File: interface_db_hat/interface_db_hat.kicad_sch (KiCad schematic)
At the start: 37 parts, among them J10 Conn_02x06_Counter_Clockwise, J2 DF19G-20P-1H52, J3 Conn_02x06_Counter_Clockwise, J6 Conn_01x04_Pin, J9 Conn_02x06_Counter_Clockwise, Q1 BC817

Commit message: ordered
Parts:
- C31, C34, C46: footprint Capacitor_SMD:C_0603_1608Metric_Pad1.08x0.95mm_HandSolder -> Capacitor_SMD:C_0805_2012Metric
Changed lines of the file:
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@@
 			)
 		)
-		(property "Footprint" "Capacitor_SMD:C_0603_1608Metric_Pad1.08x0.95mm_HandSolder"
+		(property "Footprint" "Capacitor_SMD:C_0805_2012Metric"
 			(at 147.0152 157.48 0)
 			(hide yes)
@@
 			)
 		)
-		(property "Footprint" "Capacitor_SMD:C_0603_1608Metric_Pad1.08x0.95mm_HandSolder"
+		(property "Footprint" "Capacitor_SMD:C_0805_2012Metric"
 			(at 84.7852 180.34 0)
 			(hide yes)
@@
 			)
 		)
-		(property "Footprint" "Capacitor_SMD:C_0603_1608Metric_Pad1.08x0.95mm_HandSolder"
+		(property "Footprint" "Capacitor_SMD:C_0805_2012Metric"
 			(at 84.7852 133.35 0)
 			(hide yes)

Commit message: update
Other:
- added sheet photodiode (photodiode.kicad_sch)
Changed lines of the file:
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@@
+	)
+	(sheet
+		(at 110.49 170.815)
+		(size 46.99 21.59)
+		(exclude_from_sim no)
+		(in_bom yes)
+		(on_board yes)
+		(dnp no)
+		(fields_autoplaced yes)
+		(stroke
+			(width 0.1524)
+			(type solid)
+		)
+		(fill
+			(color 0 0 0 0)
+		)
+		(property "Sheetname" "photodiode"
+			(at 110.49 170.1034 0)
+			(show_name no)
+			(do_not_autoplace no)
+			(effects
+				(font
+					(size 1.27 1.27)
+				)
+				(justify left bottom)
+			)
+		)
+		(property "Sheetfile" "photodiode.kicad_sch"
+			(at 110.49 192.9896 0)
+			(show_name no)
+			(do_not_autoplace no)
+			(effects
+				(font
+					(size 1.27 1.27)
+				)
+				(justify left top)
+			)
+		)
+		(instances
+			(project "interface_db_hat"
+				(path "/e63e39d7-6ac0-4ffd-8aa3-1841a4541b55"
+					(page "5")
+				)
+			)
+		)
 	)
 	(sheet

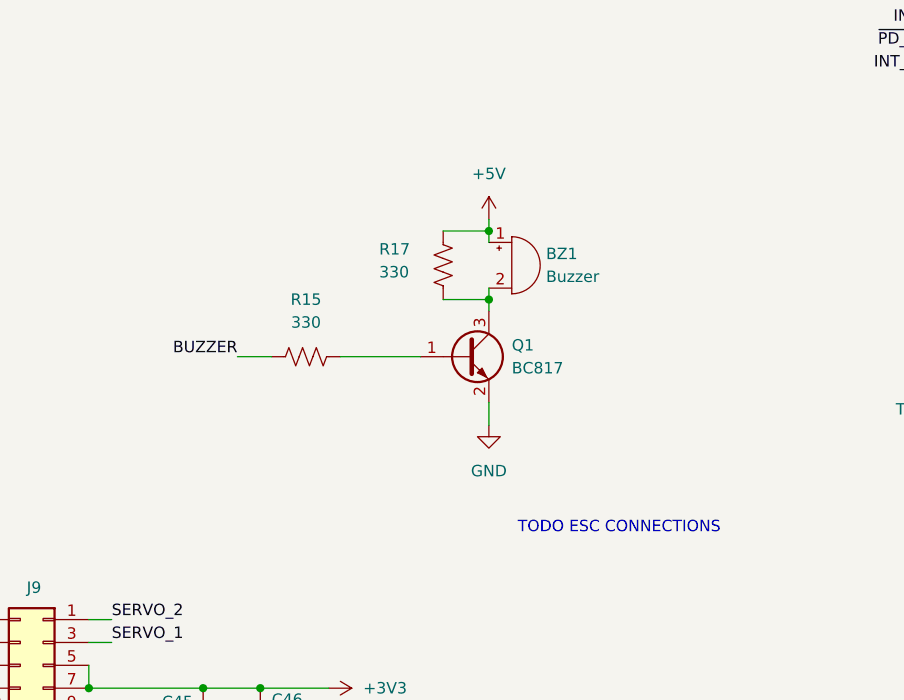
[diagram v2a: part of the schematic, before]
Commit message: starting interface layout
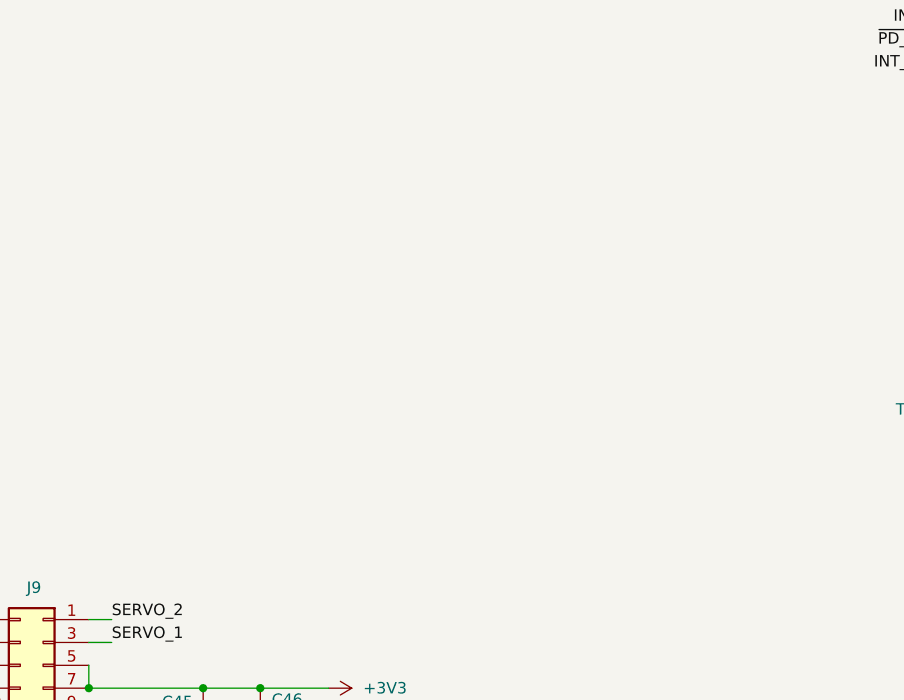
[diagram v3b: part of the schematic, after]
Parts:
- removed BZ1: Buzzer, Buzzer_Beeper:Buzzer_CUI_CPT-9019S-SMT, symbol Device:Buzzer
- removed Q1: BC817, Package_TO_SOT_SMD:SOT-23_Handsoldering, symbol Transistor_BJT:BC817
- removed R15, R17: 330, Resistor_SMD:R_0603_1608Metric_Pad0.98x0.95mm_HandSolder, symbol Device:R_US
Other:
- note removed: "TODO ESC CONNECTIONS"

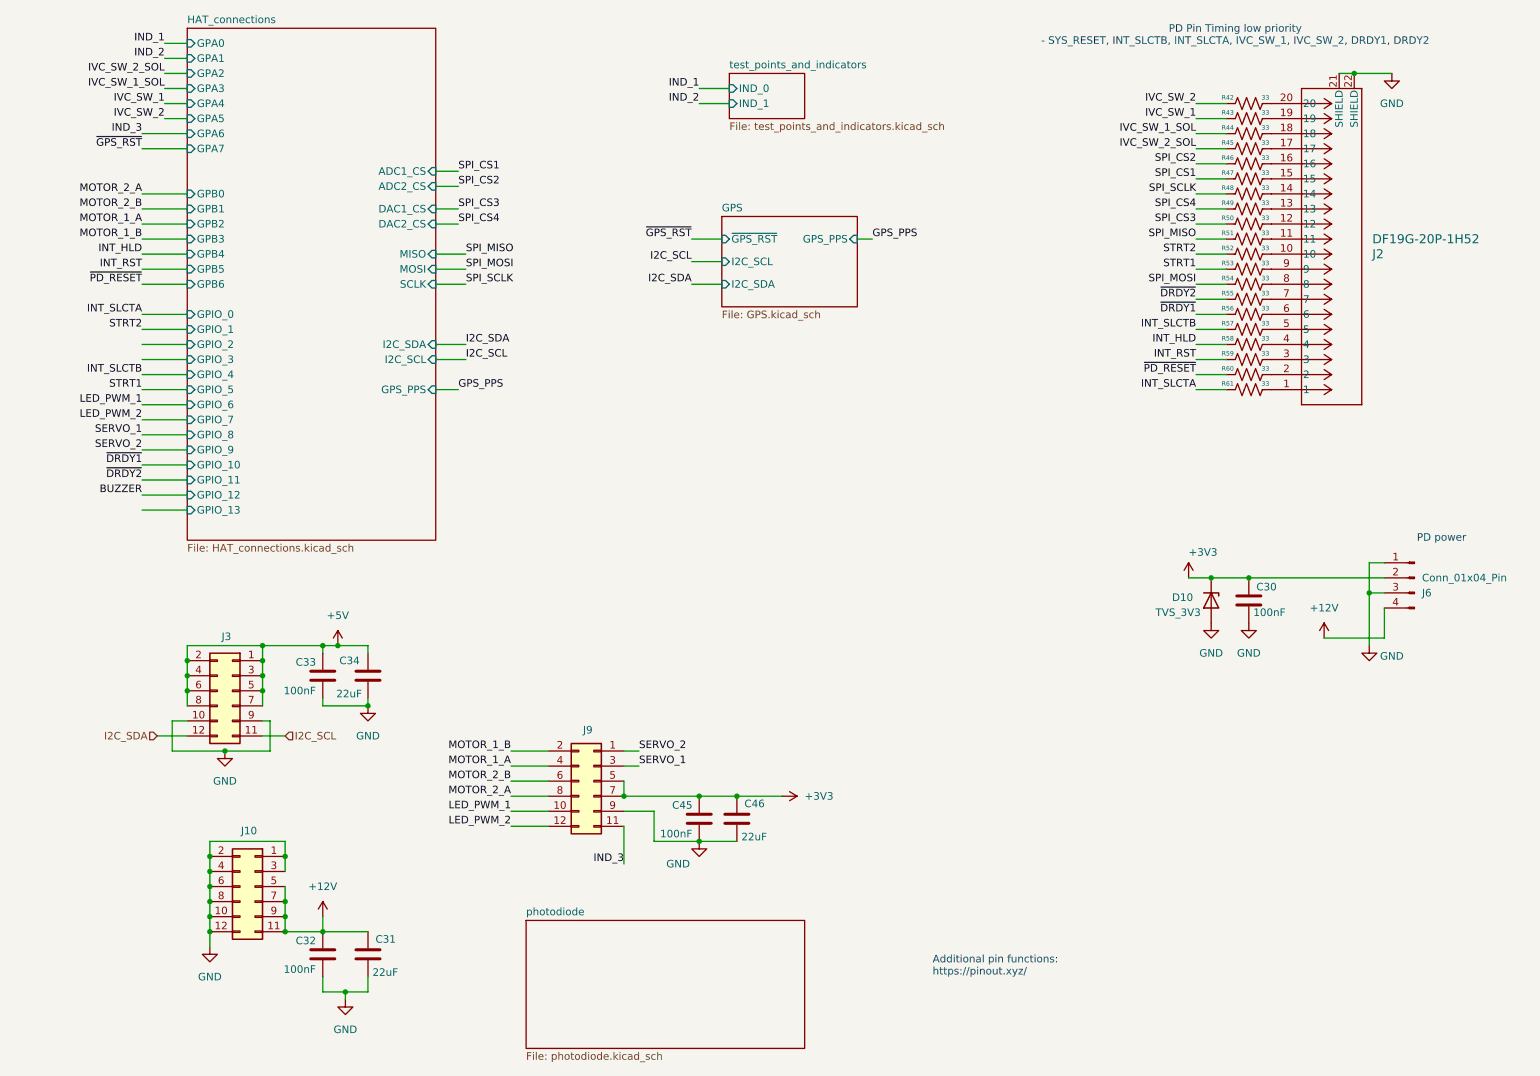
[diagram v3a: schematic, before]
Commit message: interface layout done
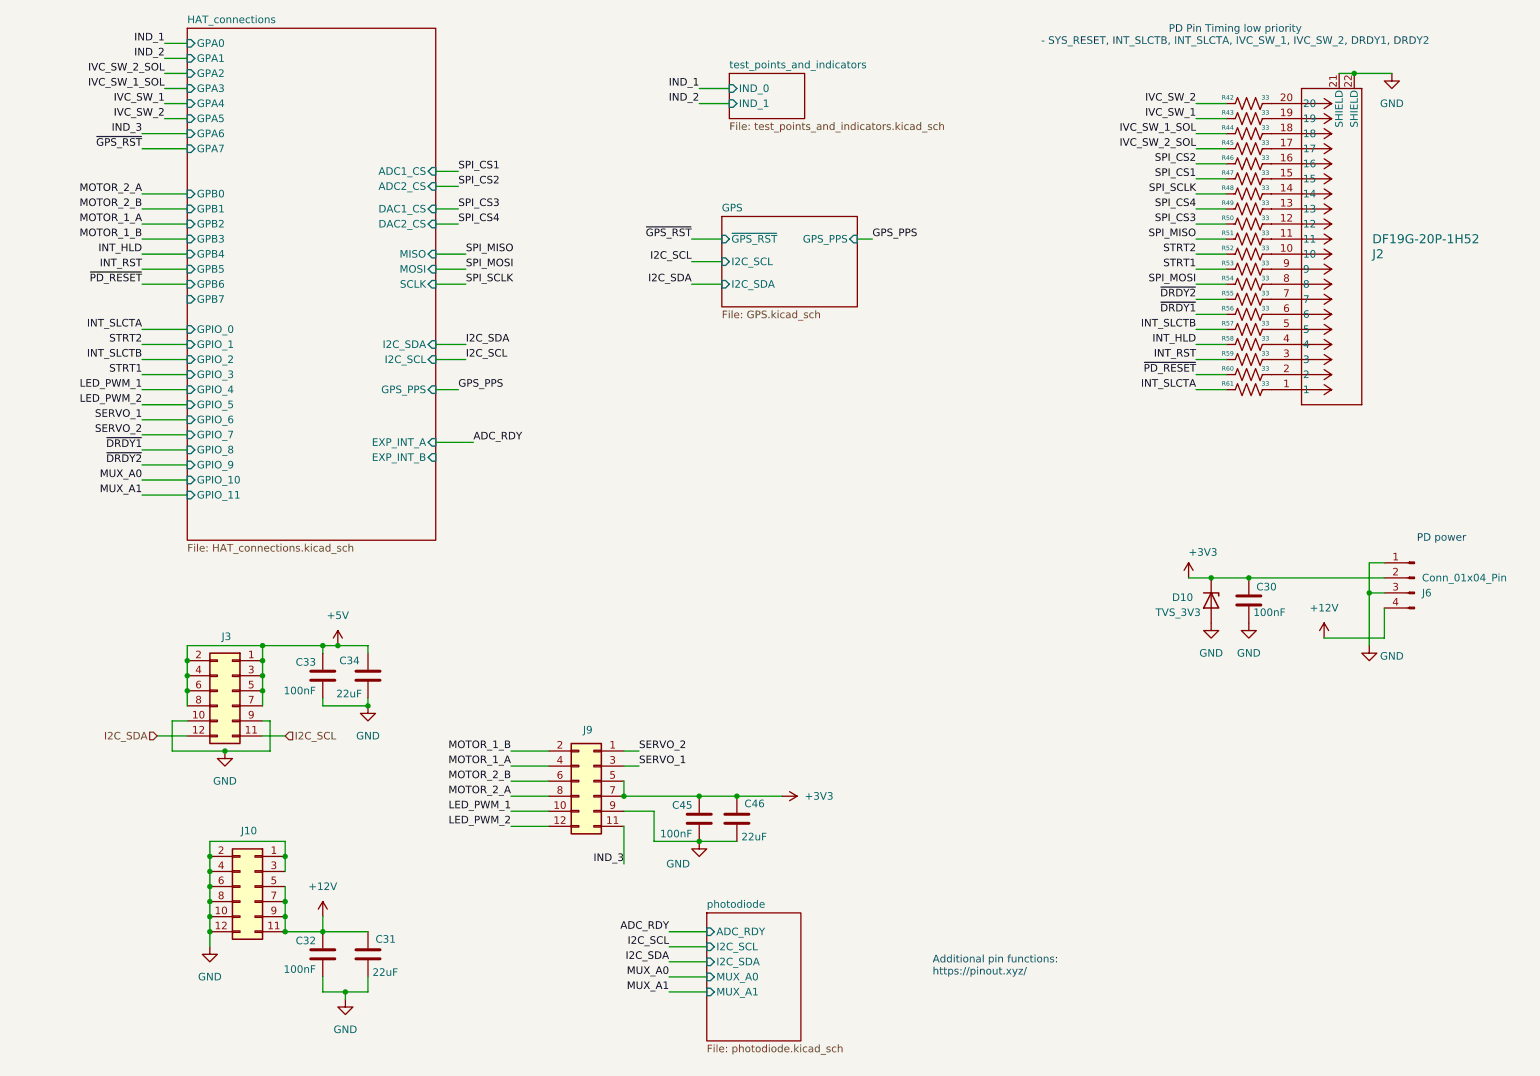
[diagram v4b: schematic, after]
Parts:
- D10: footprint Diode_SMD:D_0402_1005Metric_Pad0.77x0.64mm_HandSolder -> Diode_SMD:D_0603_1608Metric
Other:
- sheet HAT_connections ports: added EXP_INT_A, EXP_INT_B, GPB7; removed GPIO_12, GPIO_13
- sheet photodiode ports: added ADC_RDY, I2C_SCL, I2C_SDA, MUX_A0, MUX_A1; removed none

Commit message: fixed interface schematic
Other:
- sheet HAT_connections ports: added GPIO_12, GPIO_13, GPIO_14, GPIO_15, GPIO_16, GPIO_17; removed ADC1_CS, ADC2_CS, DAC1_CS, DAC2_CS

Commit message: jlc order
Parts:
- added J11, J7: Conn_01x06_Pin, Connector_JST:JST_GH_SM06B-GHS-TB_1x06-1MP_P1.25mm_Horizontal, symbol Connector:Conn_01x06_Pin
- added R1, R15, R17, R18, R19, R20, R5, R6: 33, Resistor_SMD:R_0603_1608Metric, symbol Device:R_US
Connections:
- net +5V: now also J11.1 (Pin_1), J7.1 (Pin_1)
- net GND: now also J11.2 (Pin_2), J7.2 (Pin_2)
- net MUX_A0: now also R18.1
- net MUX_A1: now also R5.1
- net SPI_MISO: now also R15.1, R20.1
- net SPI_MOSI: now also R19.1, R6.1
- net SPI_SCLK: now also R1.1, R17.1
- new net: J11.5 (Pin_5), R5.2
- new net: J11.6 (Pin_6), R1.2
- new net: J7.4 (Pin_4), R19.2
- new net: J11.3 (Pin_3), R15.2
- new net: J7.5 (Pin_5), R18.2
- new net: J7.6 (Pin_6), R17.2
- new net: J11.4 (Pin_4), R6.2
- new net: J7.3 (Pin_3), R20.2
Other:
- removed sheet photodiode
